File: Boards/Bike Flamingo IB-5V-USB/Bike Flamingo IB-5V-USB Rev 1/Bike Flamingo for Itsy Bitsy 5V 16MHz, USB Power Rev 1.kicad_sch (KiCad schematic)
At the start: 10 parts, among them J1 Battery Connector, J2 Button Board Terminal, J3 Button Board Terminal, U1 Adafruit_ItsyBitsy_5V_16MHz

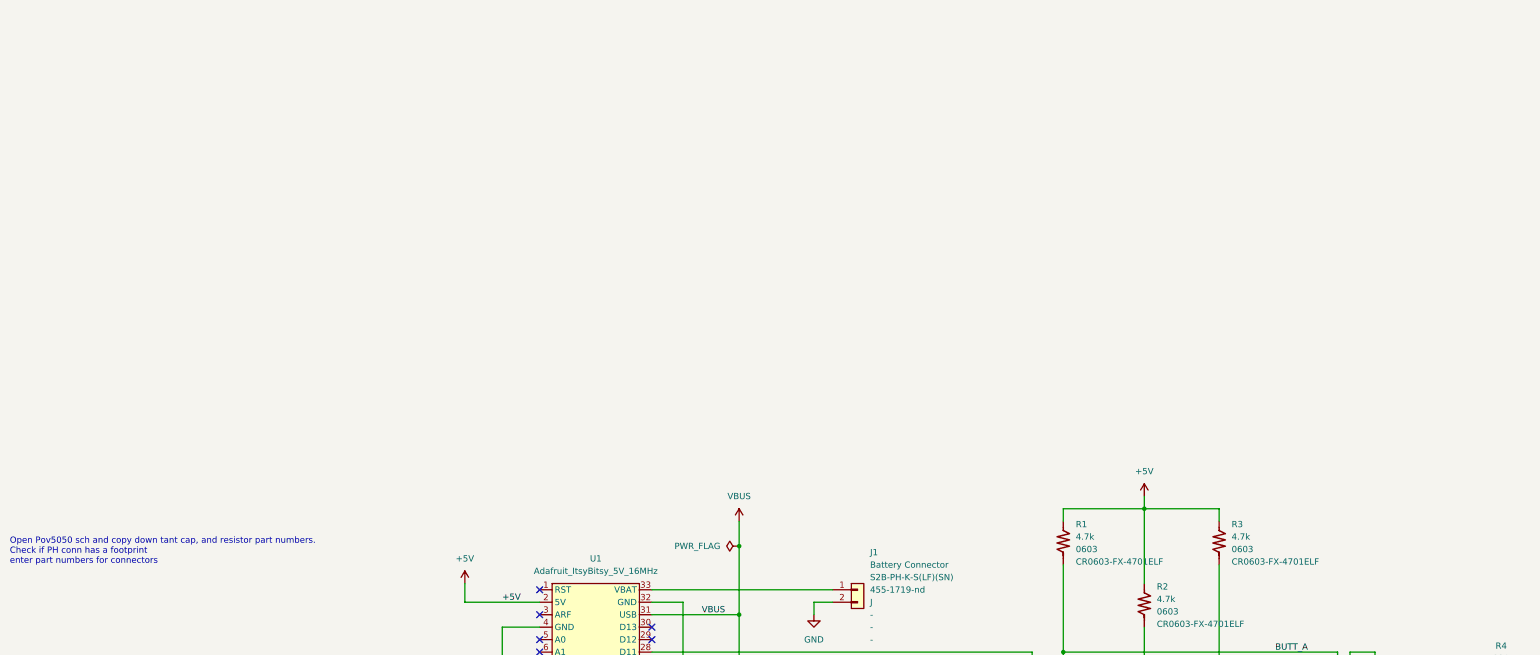
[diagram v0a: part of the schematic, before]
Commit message: Added some notes on power: the battery connector is not likely to be useful
Since if USB is unplugged, the only route to the LED VCC (VBUS) is through the 5 V regulator. This is also true if a battery backpack is used.

Does it make sense to put the batt connector on the VUSB line? Not really, because then the Arduino just sees unregulated batt... which is OK for a LiPo I guess.

Does it make sense to change the LEDs to use VBAT? With VBAT and no USB present, the LEDS get direct battery and the arduino gets regulated output. With USB and no VBAT the LEDs dont see VBUS unless a battery backpack is used.
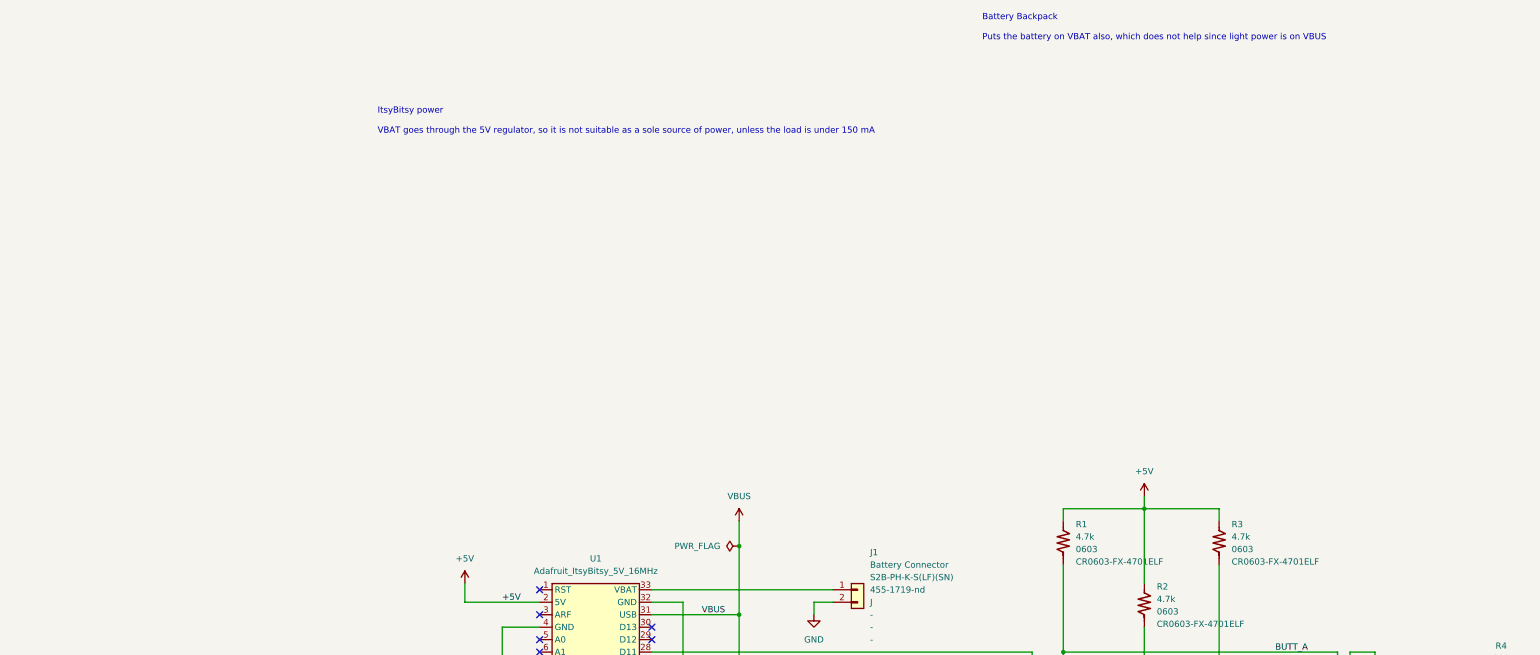
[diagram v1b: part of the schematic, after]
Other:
- note added: "Battery Backpack Puts the battery on VBAT also, which does not help since light power is on VBUS"
- note added: "ItsyBitsy power VBAT goes through the 5V regulator, so it is not suitable as a sole source of power, unless the load is under 150 mA"
- note removed: "Open Pov5050 sch and copy down tant cap, and resistor part numbers. Check if PH conn has a footprint enter part numbers for connectors"

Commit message: Preprocessor commenitng out for board type
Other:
- note added: "Since if USB is unplugged, the only route to the LED VCC (VBUS) is through the 5 V regulator. This is also true if a battery backpack is used. Does it make sense to put the batt connector on the VUSB line? Not really, because then the Arduino just sees unregulated batt... which is OK for a LiPo I guess. Does it make sense to change the LEDs to use VBAT? With VBAT and no USB present, the LEDS get 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"
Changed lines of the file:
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@@
     (stroke (width 0) (type default) (color 0 0 0 0))
   )
-  (image (at 33.02 -26.67)
+  (image (at 50.8 170.18)
     (data
       iVBORw0KGgoAAAANSUhEUgAAAykAAAI3CAIAAAAQo4NiAAAAA3NCSVQICAjb4U/gAAAACXBIWXMA
@@
     )
   )
-  (image (at 184.15 -35.56) (scale 1.58632)
+  (image (at 60.96 -35.56) (scale 1.58632)
     (data
       iVBORw0KGgoAAAANSUhEUgAAA58AAAHsCAIAAADaWo5tAAAAA3NCSVQICAjb4U/gAAAACXBIWXMA
@@
   )
   (text "ItsyBitsy power\n\nVBAT goes through the 5V regulator, so it is not suitable as a sole source of power, unless the load is under 150 mA\n"
-    (at 0 -53.34 0)
+    (at 16.51 143.51 0)
+    (effects (font (size 1.27 1.27)) (justify left bottom))
+  )
+  (text "Since if USB is unplugged, the only route to the LED VCC (VBUS) is through the 5 V regulator. This is also true if a battery backpack is used. \n\nDoes it make sense to put the batt connector on the VUSB line? Not really, because then the Arduino just sees unregulated batt... which is OK for a LiPo I guess.\n\nDoes it make sense to change the LEDs to use VBAT? With VBAT and no USB present, the LEDS get direct battery and the arduino gets regulated output. With USB and no VBAT the LEDs dont see VBUS unless a battery backpack is used. "
+    (at 125.73 -3.81 0)
     (effects (font (size 1.27 1.27)) (justify left bottom))
   )
   (text "Battery Backpack\n\nPuts the battery on VBAT also, which does not help since light power is on VBUS"
-    (at 123.19 -72.39 0)
+    (at 0 -71.12 0)
     (effects (font (size 1.27 1.27)) (justify left bottom))
   )
@@
     )
     (property "Website" "https://www.digikey.com/en/products/detail/kyocera-avx/TPSF107M016R0200/3068751" (id 10) (at 251.46 108.7881 0)
-      (effects (font (size 1.27 1.27)) (justify left))
+      (effects (font (size 1.27 1.27)) (justify left) hide)
     )
     (property "Description" "-" (id 11) (at 251.46 111.3281 0)
